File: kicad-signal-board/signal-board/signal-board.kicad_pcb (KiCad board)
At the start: 2 copper layers, 1 part, among them U1 ESP32-DEVKITC-32D

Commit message: signal board stufffffff
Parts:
- added D1: WS2812, LED_SMD:LED_WS2812_PLCC6_5.0x5.0mm_P1.6mm, F.Cu at (193.0, 90.2)
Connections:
- U1 pad 14: GNDREF -> GND
- U1 pad 20: Net-(U1-Pad20) -> GND
- U1 pad 26: Net-(U1-Pad26) -> GND

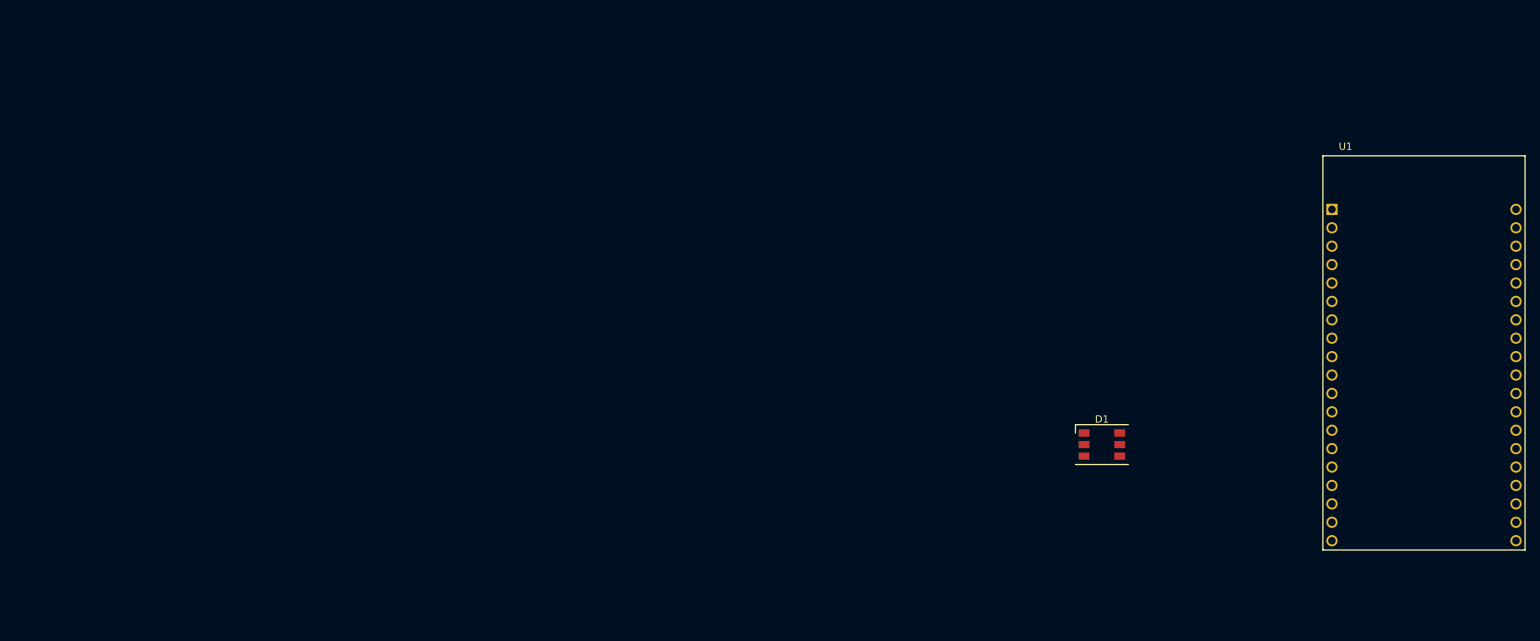
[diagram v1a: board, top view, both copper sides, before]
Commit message: Copied power supply circuit into signal board schematic, initial creation of PCB
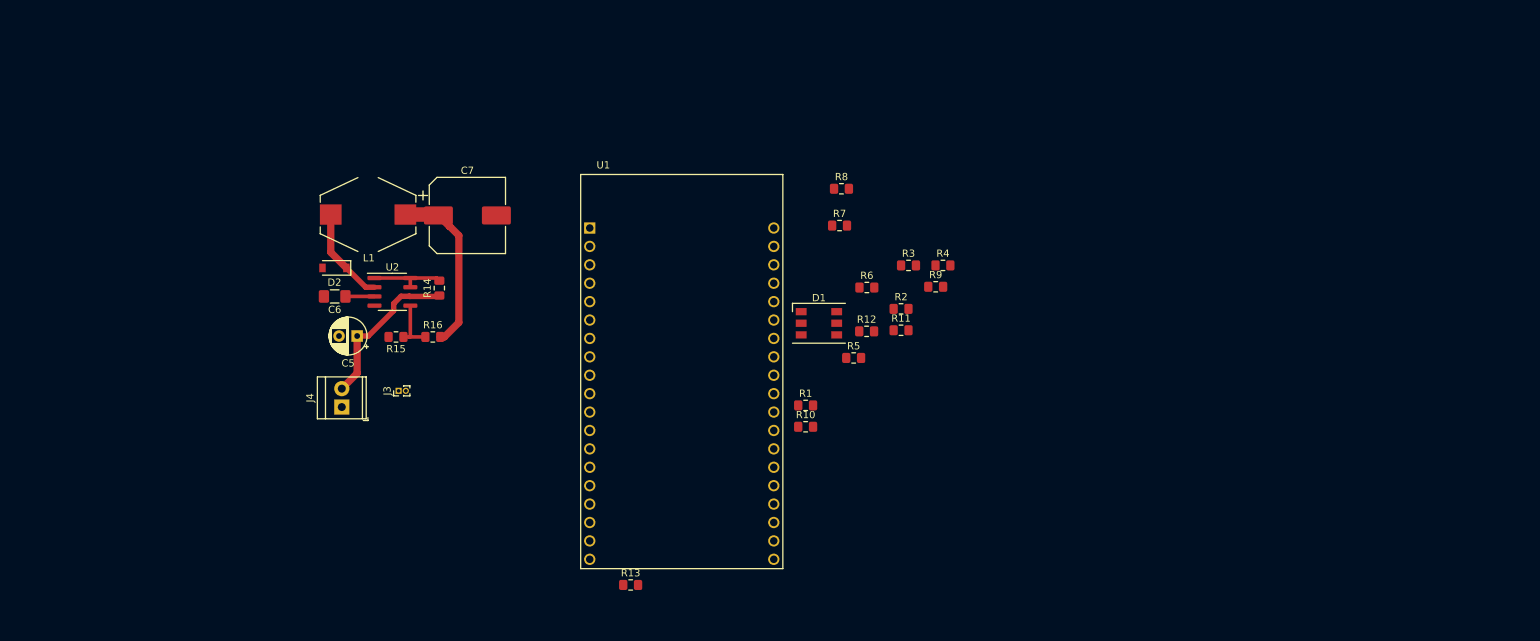
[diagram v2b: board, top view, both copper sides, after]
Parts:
- added C5: 100uF, Capacitor_THT:CP_Radial_D5.0mm_P2.50mm, F.Cu at (90.3, 75.2)
- added C6: 470pF, Capacitor_SMD:C_1206_3216Metric_Pad1.42x1.75mm_HandSolder, F.Cu at (87.2, 69.7)
- added C7: 220uF, Capacitor_SMD:CP_Elec_10x10, F.Cu at (105.5, 58.5)
- added D2: 1N5819, Diode_SMD:D_SOD-123, F.Cu at (87.1, 65.8)
- added J3: 5V Pwr Conn, Connector_PinHeader_1.00mm:PinHeader_1x02_P1.00mm_Vertical, F.Cu at (96.0, 82.8)
- added J4: 24V Screw Term, TerminalBlock_TE-Connectivity:TerminalBlock_TE_282834-2_1x02_P2.54mm_Horizontal, F.Cu at (88.1, 85.0)
- added L1: 220uH, Inductor_SMD:L_Bourns-SRR1005, F.Cu at (91.8, 58.4)
- added R1: 1k, Resistor_SMD:R_0805_2012Metric_Pad1.15x1.40mm_HandSolder, F.Cu at (152.2, 84.8)
- added R10: 100, Resistor_SMD:R_0805_2012Metric_Pad1.15x1.40mm_HandSolder, F.Cu at (152.2, 87.7)
- added R11: 100, Resistor_SMD:R_0805_2012Metric_Pad1.15x1.40mm_HandSolder, F.Cu at (165.3, 74.4)
- added R12: 100, Resistor_SMD:R_0805_2012Metric_Pad1.15x1.40mm_HandSolder, F.Cu at (160.6, 74.5)
- added R13: 100, Resistor_SMD:R_0805_2012Metric_Pad1.15x1.40mm_HandSolder, F.Cu at (128.0, 109.5)
- added R14: 0.33 ohms, Resistor_SMD:R_0805_2012Metric_Pad1.15x1.40mm_HandSolder, F.Cu at (101.6, 68.6)
- added R15: 1.2K, Resistor_SMD:R_0805_2012Metric_Pad1.15x1.40mm_HandSolder, F.Cu at (95.6, 75.3)
- added R16: 3.8K, Resistor_SMD:R_0805_2012Metric_Pad1.15x1.40mm_HandSolder, F.Cu at (100.7, 75.3)
- added R2: 10k, Resistor_SMD:R_0805_2012Metric_Pad1.15x1.40mm_HandSolder, F.Cu at (165.3, 71.4)
- added R3: 1k, Resistor_SMD:R_0805_2012Metric_Pad1.15x1.40mm_HandSolder, F.Cu at (166.4, 65.4)
- added R4: 150, Resistor_SMD:R_0805_2012Metric_Pad1.15x1.40mm_HandSolder, F.Cu at (171.1, 65.4)
- added R5: 10k, Resistor_SMD:R_0805_2012Metric_Pad1.15x1.40mm_HandSolder, F.Cu at (158.8, 78.2)
- added R6: 100, Resistor_SMD:R_0805_2012Metric_Pad1.15x1.40mm_HandSolder, F.Cu at (160.6, 68.5)
- added R7: 100, Resistor_SMD:R_0805_2012Metric_Pad1.15x1.40mm_HandSolder, F.Cu at (156.8, 59.9)
- added R8: 100, Resistor_SMD:R_0805_2012Metric_Pad1.15x1.40mm_HandSolder, F.Cu at (157.1, 54.9)
- added R9: 100, Resistor_SMD:R_0805_2012Metric_Pad1.15x1.40mm_HandSolder, F.Cu at (170.1, 68.4)
- added U2: MC33063AD, Package_SO:SOIC-8_3.9x4.9mm_P1.27mm, F.Cu at (95.1, 69.1)
- moved U1 102.5 mm to (135.1, 80.0)
- moved D1 42.5 mm to (154.0, 73.4)
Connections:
- net 5v renamed +5V
- D1 pad 6: GNDREF -> GND
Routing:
- net +5V: track 0.00 -> 24.0 mm
- net +24V: track 0.00 -> 22.4 mm
- net Net-(D2-Pad1): track 0.00 -> 13.2 mm
- net Net-(R14-Pad2): track 0.00 -> 10.4 mm
- net Net-(R15-Pad1): track 0.00 -> 7.37 mm
- net Net-(C6-Pad1): track 0.00 -> 4.00 mm

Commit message: More footprints and rough layout of pcb
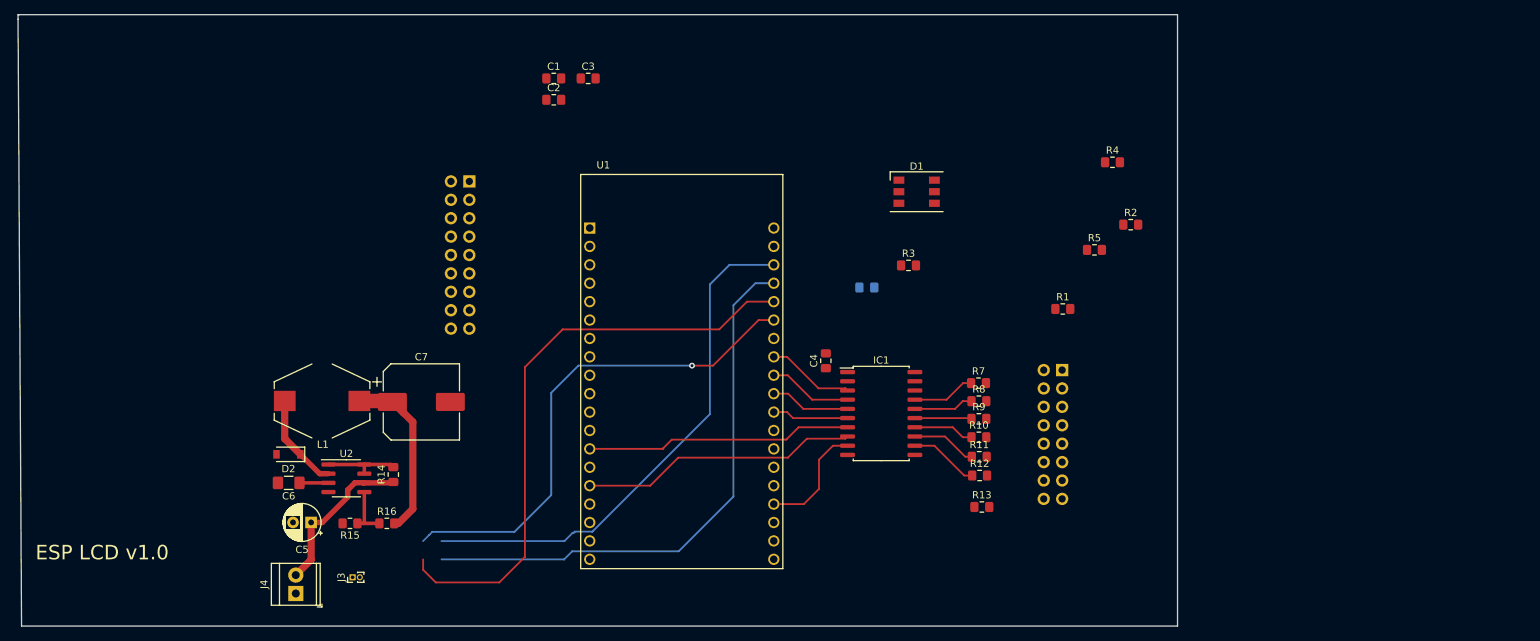
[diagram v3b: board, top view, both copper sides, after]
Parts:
- added C1: 0.1µF, Capacitor_SMD:C_0805_2012Metric_Pad1.15x1.40mm_HandSolder, F.Cu at (117.4, 39.6)
- added C2: 0.1µF, Capacitor_SMD:C_0805_2012Metric_Pad1.15x1.40mm_HandSolder, F.Cu at (117.4, 42.6)
- added C3: 0.1µF, Capacitor_SMD:C_0805_2012Metric_Pad1.15x1.40mm_HandSolder, F.Cu at (122.1, 39.6)
- added C4: 1uF, Capacitor_SMD:C_0805_2012Metric_Pad1.15x1.40mm_HandSolder, F.Cu at (154.9, 78.6)
- added IC1: 74HCT245, Package_SO:SOIC-20W_7.5x12.8mm_P1.27mm, F.Cu at (162.6, 85.9)
- added J1: Conn_02x09_Odd_Even, Connector_PinHeader_2.54mm:PinHeader_2x09_P2.54mm_Vertical, B.Cu at (105.7, 53.8)
- added J2: Conn_02x08_Odd_Even, Connector_PinHeader_2.54mm:PinHeader_2x08_P2.54mm_Vertical, B.Cu at (187.6, 79.9)
- R6: moved to B.Cu
- moved R13 49.6 mm to (176.5, 98.8)
- moved R1 37.9 mm to (187.6, 71.5)
- moved R5 36.4 mm to (192.0, 63.3)
- moved R8 34.9 mm to (176.1, 84.2)
- moved R2 33.8 mm to (197.0, 59.8)
- moved R7 29.0 mm to (176.0, 81.7)
- moved R4 27.4 mm to (194.5, 51.2)
- moved U2 26.5 mm to (88.8, 94.8)
- moved C5 26.5 mm to (83.9, 100.9)
- moved C6 26.5 mm to (80.8, 95.5)
- moved D2 26.5 mm to (80.8, 91.5)
- moved J4 26.5 mm to (81.8, 110.7)
- moved C7 26.5 mm to (99.1, 84.3)
- moved J3 26.5 mm to (89.6, 108.5)
- moved L1 26.5 mm to (85.4, 84.2)
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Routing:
- net Net-(J1-Pad18): track 0.00 -> 81.9 mm
- net Net-(J1-Pad17): track 0.00 -> 77.1 mm
- net Net-(J1-Pad15): track 0.00 -> 72.1 mm
- net Net-(J1-Pad16): track 0.00 -> 69.3 mm, vias 0 -> 1
- net Net-(IC1-Pad8): track 0.00 -> 38.4 mm
- net Net-(IC1-Pad7): track 0.00 -> 36.9 mm
- net Net-(IC1-Pad9): track 0.00 -> 15.9 mm
- net Net-(IC1-Pad3): track 0.00 -> 12.1 mm
- net Net-(IC1-Pad4): track 0.00 -> 11.6 mm
- net Net-(IC1-Pad5): track 0.00 -> 11.0 mm
- net Net-(IC1-Pad6): track 0.00 -> 10.5 mm
- net Net-(IC1-Pad12): track 0.00 -> 9.61 mm
- net Net-(IC1-Pad13): track 0.00 -> 9.01 mm
- net Net-(IC1-Pad17): track 0.00 -> 8.70 mm
- net Net-(IC1-Pad14): track 0.00 -> 8.37 mm
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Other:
- board outline added: 160 x 84.4 mm
- board text added: "ESP LCD v1.0"

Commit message: traces 1.0 done
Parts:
- added SW1: SW_MEC_5G, PTS525SM15SMTR2LFS:SW_PTS525SM15SMTR2LFS, F.Cu at (164.8, 56.5)
- added SW2: SW_MEC_5G, PTS525SM15SMTR2LFS:SW_PTS525SM15SMTR2LFS, F.Cu at (164.8, 72.8)
- J1, J2, R6: moved to F.Cu
- moved C3 53.8 mm to (169.0, 66.0), turned to 90 degrees
- moved C2 50.1 mm to (158.0, 72.0)
- moved C1 44.2 mm to (158.0, 57.0)
- moved R2 39.4 mm to (158.0, 54.5), turned to 180 degrees
- moved R4 38.5 mm to (158.3, 64.4), turned to -90 degrees
- moved J3 36.7 mm to (110.0, 78.0), turned to -90 degrees
- moved R5 34.6 mm to (158.0, 69.5), turned to 180 degrees
- moved J4 32.5 mm to (113.5, 103.7), turned to 180 degrees
- moved R1 32.0 mm to (158.0, 59.5), turned to 180 degrees
- moved R6 30.0 mm to (170.5, 96.8), turned to -90 degrees
- moved J2 29.1 mm to (170.5, 103.5), turned to -90 degrees
- moved R15 25.9 mm to (115.0, 98.0), turned to 0 degrees
- moved R13 23.6 mm to (153.0, 96.8), turned to -90 degrees
- moved R16 21.7 mm to (115.0, 94.5), turned to 90 degrees
- moved R12 20.8 mm to (155.5, 96.8), turned to -90 degrees
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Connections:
- J1 pad 1: GND -> Net-(J1-Pad1)
- J1 pad 15: Net-(J1-Pad15) -> GND
- J1 pad 17: Net-(J1-Pad17) -> GND
- J1 pad 3: GND -> Net-(J1-Pad3)
- J2 pad 1: Net-(J2-Pad1) -> Net-(D1-Pad1)
- R6 pad 2: Net-(J2-Pad1) -> Net-(D1-Pad2)
- U1 pad 10: Net-(J1-Pad12) -> Net-(J1-Pad16)
- U1 pad 11: Net-(J1-Pad14) -> Net-(J1-Pad18)
- U1 pad 12: Net-(D1-Pad2) -> Net-(U1-Pad12)
- U1 pad 22: Net-(J1-Pad15) -> Net-(J1-Pad1)
- U1 pad 23: Net-(J1-Pad17) -> Net-(J1-Pad3)
- U1 pad 24: Net-(J1-Pad18) -> Net-(J1-Pad4)
- U1 pad 25: Net-(J1-Pad16) -> Net-(J1-Pad2)
- U1 pad 3: Net-(J1-Pad2) -> Net-(J1-Pad6)
- U1 pad 4: Net-(J1-Pad4) -> Net-(J1-Pad8)
- U1 pad 5: Net-(C2-Pad1) -> Net-(C1-Pad1)
- U1 pad 6: Net-(C1-Pad1) -> Net-(C2-Pad1)
- U1 pad 7: Net-(J1-Pad6) -> Net-(J1-Pad10)
- U1 pad 8: Net-(J1-Pad8) -> Net-(J1-Pad12)
- U1 pad 9: Net-(J1-Pad10) -> Net-(J1-Pad14)
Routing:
- net +5V: track 24.0 -> 176.7 mm, vias 0 -> 4
- net Net-(J1-Pad17): track 77.1 -> 0.00 mm
- net Net-(J1-Pad15): track 72.1 -> 0.00 mm
- net Net-(C1-Pad1): track 0.00 -> 51.7 mm
- net Net-(C2-Pad1): track 0.00 -> 43.4 mm
- net Net-(D1-Pad1): track 0.00 -> 42.0 mm, vias 0 -> 1
- net Net-(J1-Pad3): track 0.00 -> 41.6 mm
- net Net-(J1-Pad4): track 0.00 -> 40.4 mm
- net Net-(J1-Pad18): track 81.9 -> 43.3 mm
- net Net-(J1-Pad2): track 0.00 -> 37.2 mm
- net Net-(D1-Pad2): track 0.00 -> 36.3 mm, vias 0 -> 2
- net Net-(J1-Pad1): track 0.00 -> 35.1 mm
- net Net-(J1-Pad14): track 0.00 -> 32.0 mm
- net Net-(IC1-Pad2): track 0.00 -> 31.8 mm, vias 0 -> 1
- net Net-(J1-Pad16): track 69.3 -> 39.1 mm, vias 1 -> 0
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- added copper zone on F.Cu, net GND
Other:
- board size 160 x 84.4 mm -> 83.6 x 61 mm
- board text added: "+ -"
- board text added: "12"
- board text added: "13"
- board text added: "15"
- board text added: "17"
- board text added: "18"
- board text added: "19"
- board text added: "23"
- board text added: "25"
- board text added: "26"
- board text added: "27"
- board text added: "32"
- board text added: "33"
- board text added: "5"
- board text added: "7-24v"
- board text added: "<--- Led Outputs"
- board text added: "Alternate 5v supply"
- board text added: "ESP LED v1.0"
- board text added: "G"
- board text added: "GND"
- board text added: "GPIO"
- board text added: "GPIO 34"
- board text added: "GPIO 35"
- board text added: "Pixel [0] on GPIO 23"
- board text added: "R6-13"
- board text added: "RX"
- board text added: "SDA I2C"
- board text added: "SIG"
- board text added: "SLC"
- board text added: "TX"
- board text added: "VN"
- board text added: "VP"
- board text added: "|-----GPIO-----|"
- board text added: "|----| SENSOR"
- board text removed: "ESP LCD v1.0"

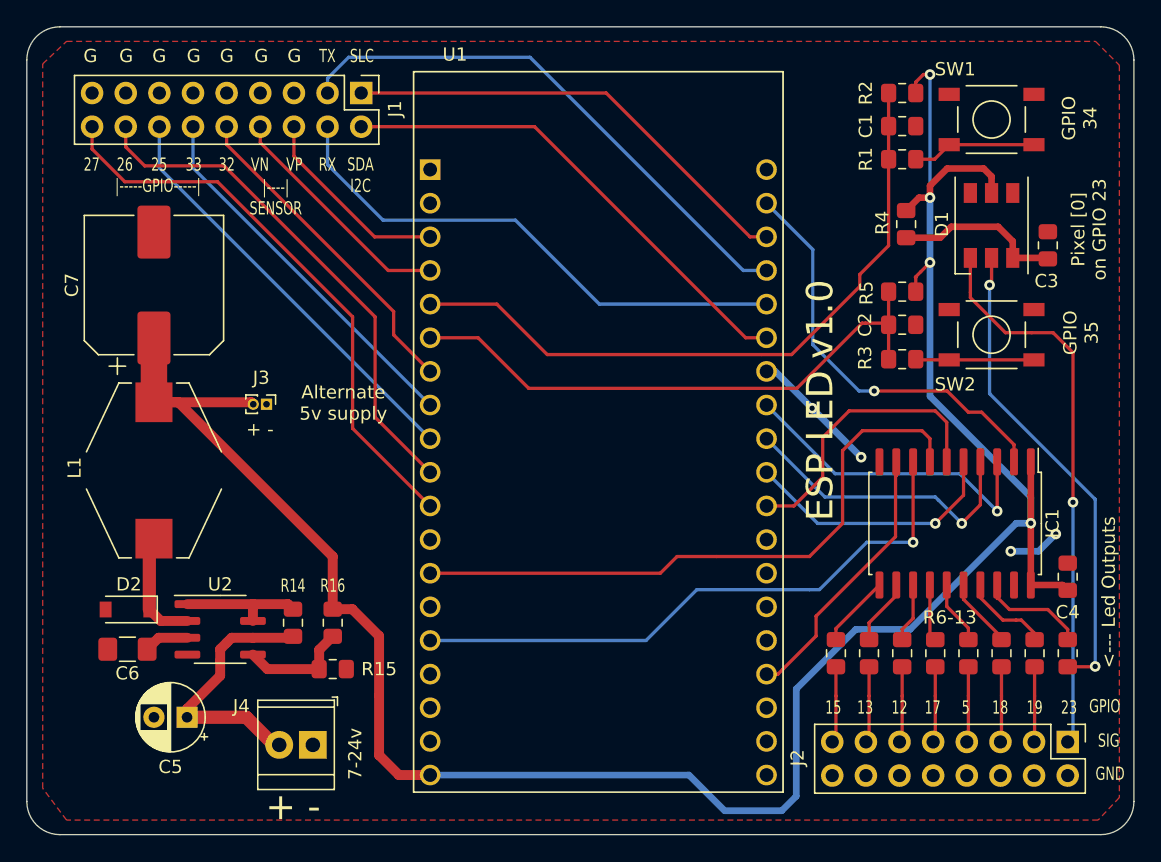
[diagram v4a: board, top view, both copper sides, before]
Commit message: Updated packages footprints and added ground plane stitching
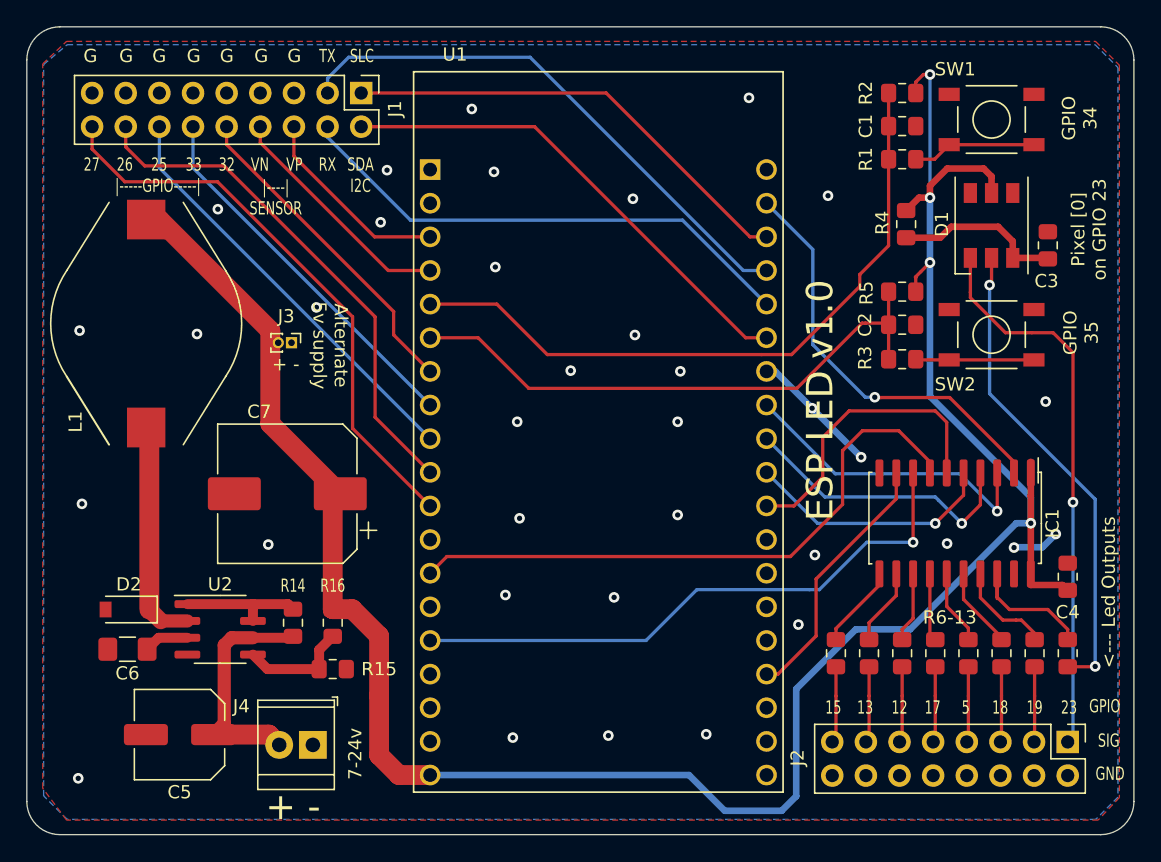
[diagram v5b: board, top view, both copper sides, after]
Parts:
- C5: footprint Capacitor_THT:CP_Radial_D5.0mm_P2.50mm -> Capacitor_SMD:C_Elec_6.3x7.7
- IC1: footprint Package_SO:SOIC-20W_7.5x12.8mm_P1.27mm -> 74HCD245:SOIC-20W_7.5x10.0mm_P1.27mm
- L1: footprint Inductor_SMD:L_Bourns-SRR1005 -> Inductor_SMD:L_Bourns_SDR1806
- moved C7 18.7 mm to (111.6, 84.8), turned to 180 degrees
- moved L1 11.1 mm to (100.9, 71.9)
- moved J3 5.01 mm to (111.9, 73.4)
- moved C5 1.43 mm to (103.4, 102.9)
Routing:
- net Net-(D2-Pad1): track 8.73 -> 17.1 mm
- net +24V: track 21.0 -> 17.9 mm
- net Net-(IC1-Pad7): track 47.4 -> 45.5 mm
- net +5V: track 176.7 -> 178.2 mm
- net Net-(J1-Pad4): track 40.4 -> 39.2 mm
- net Net-(IC1-Pad2): track 31.8 -> 31.0 mm
- net GND: track 13.8 -> 13.4 mm, vias 4 -> 35
- added copper zone on B.Cu, net GND

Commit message: A B, esp direction, holes
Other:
- outline, holes or cut-outs redrawn
- board text added: "--->"
- board text added: "A"
- board text added: "B"
- board text added: "ESP32"
- board text added: "USB"

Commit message: art and design rules
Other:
- net class Default: clearance 0.2 -> 0.254; trace_width 0.25 -> 0.254; via_dia 0.8 -> 0.508; via_drill 0.4 -> 0.254
- rule pad_to_mask_clearance: 0.05 -> 0.0508
- rule trace_clearance: 0.2 -> 0.254
- rule trace_min: 0.2 -> 0.254
- rule via_min_drill: 0.3 -> 0.254
- rule via_min_size: 0.4 -> 0.508
- board text added: "9-24v"
- board text removed: "7-24v"
